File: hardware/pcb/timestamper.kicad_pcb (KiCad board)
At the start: 2 copper layers, 75 x 100 mm, 111 parts, among them J1 Conn_Coaxial, J2 Conn_Coaxial, J3 Conn_Coaxial, J4 JTAG, J5 ISP, J6 Conn_Coaxial, J7 USB_B_Micro, U1 AP1117-33, U10 ATMEGA328-AU, U11 74HC04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

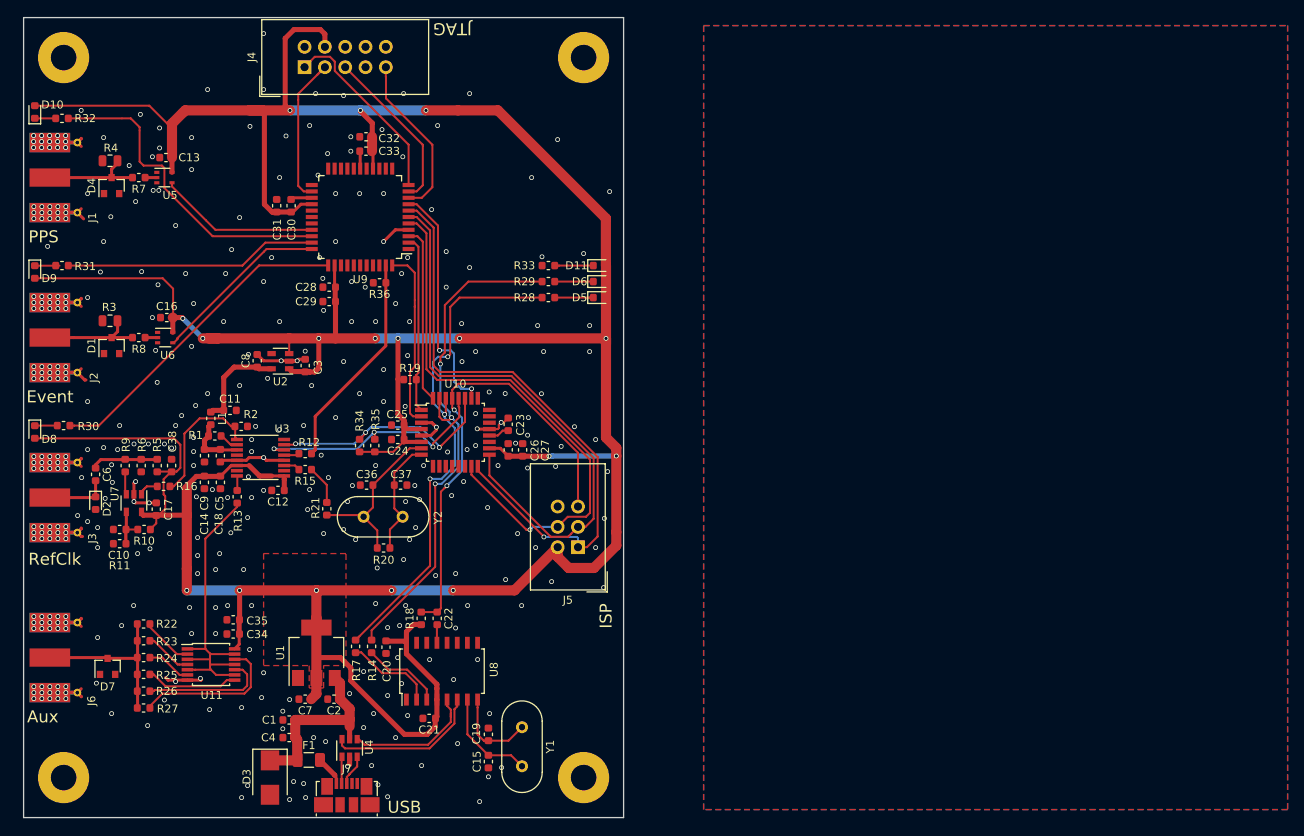
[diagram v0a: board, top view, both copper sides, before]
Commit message: Added silk-screen comments
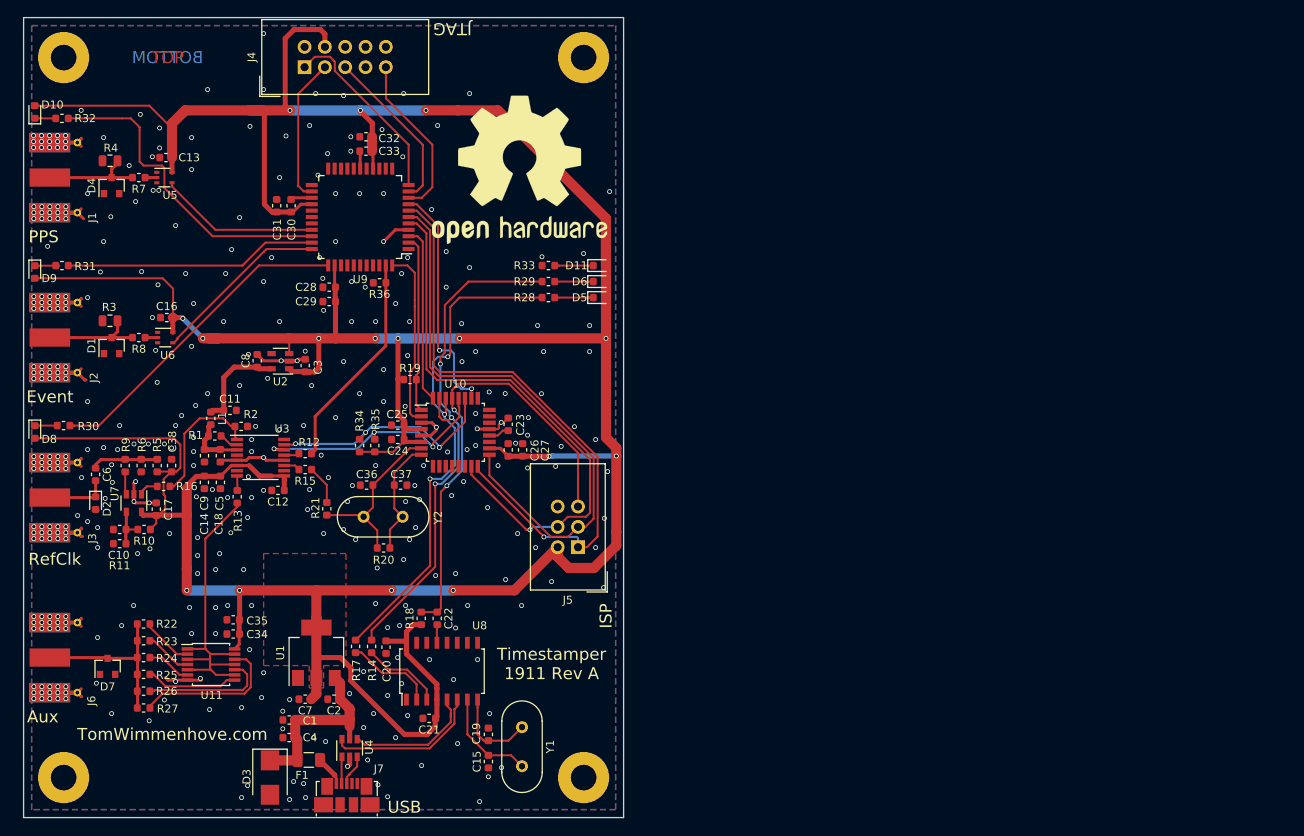
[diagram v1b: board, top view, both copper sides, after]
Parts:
- added REF**: OSHW-Logo2_24.3x20mm_SilkScreen, Symbol:OSHW-Logo2_24.3x20mm_SilkScreen, F.Cu at (112.0, 69.0)
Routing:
- net +3V3: vias 17 -> 16
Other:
- board text added: "BOTTOM"
- board text added: "TOP"
- board text added: "Timestamper 1911 Rev A"
- board text added: "TomWimmenhove.com"

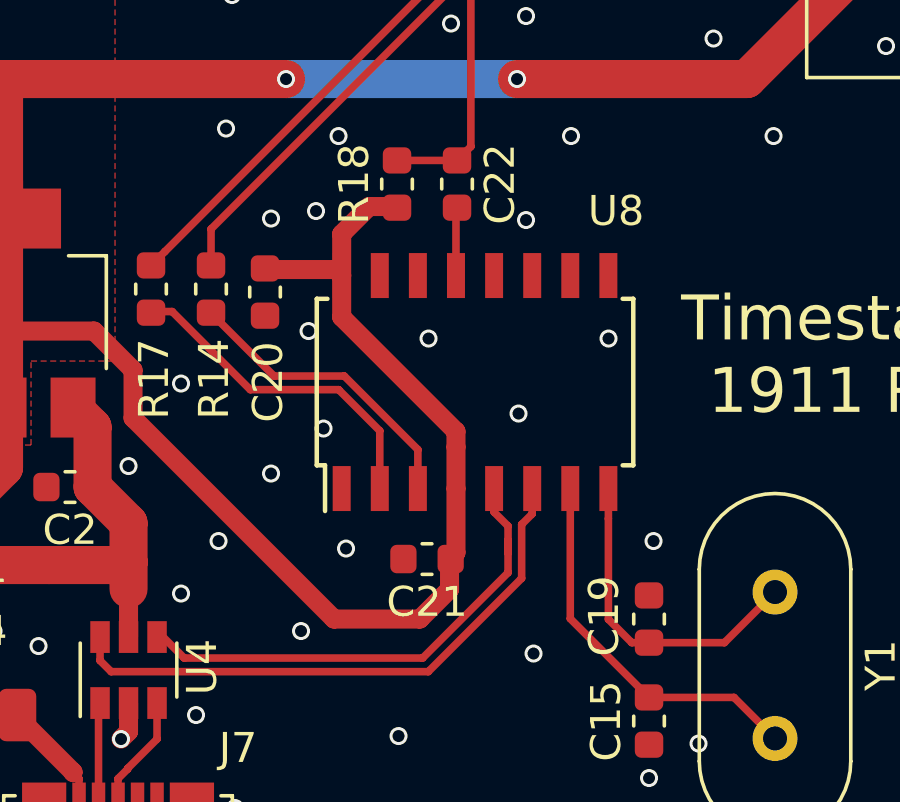
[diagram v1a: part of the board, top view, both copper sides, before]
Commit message: Fixed CH340G (U8) foot print
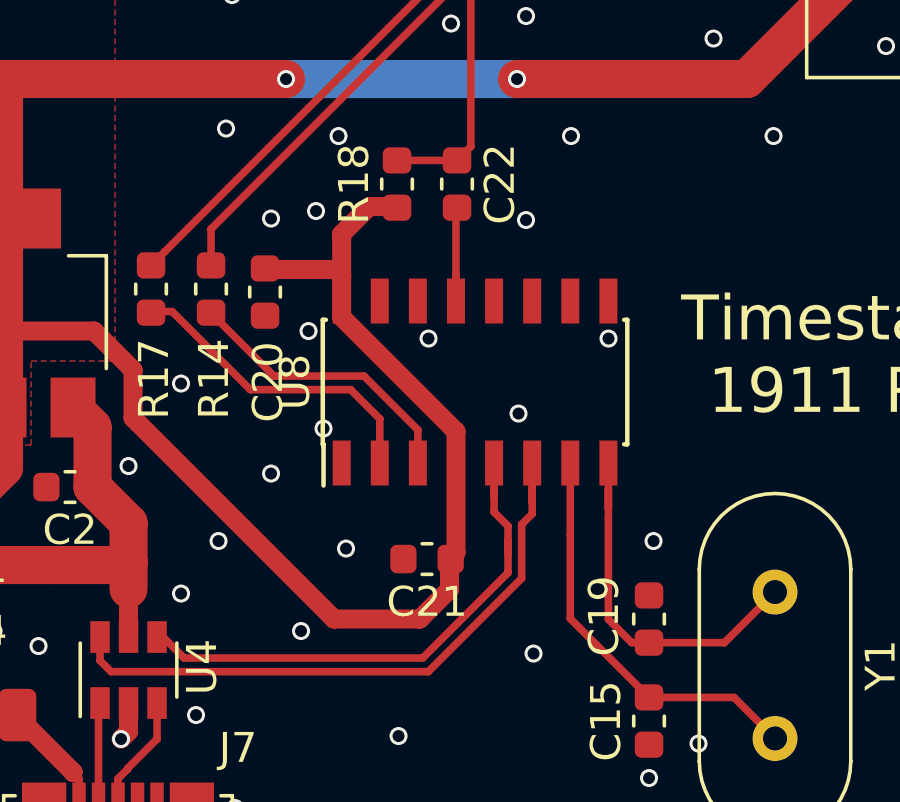
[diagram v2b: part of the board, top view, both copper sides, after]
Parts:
- U8: footprint Package_SO:SOIC-16W_5.3x10.2mm_P1.27mm -> Package_SO:SOIC-16_3.9x9.9mm_P1.27mm
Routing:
- net Net-(C19-Pad2): track 10.9 -> 12.4 mm
- net /USB_DM: track 19.4 -> 20.7 mm
- net /USB_DP: track 16.9 -> 18.0 mm
- net Net-(C22-Pad2): track 2.28 -> 3.13 mm
- net Net-(C15-Pad2): track 12.8 -> 13.7 mm
- net Net-(R17-Pad1): track 11.2 -> 10.6 mm

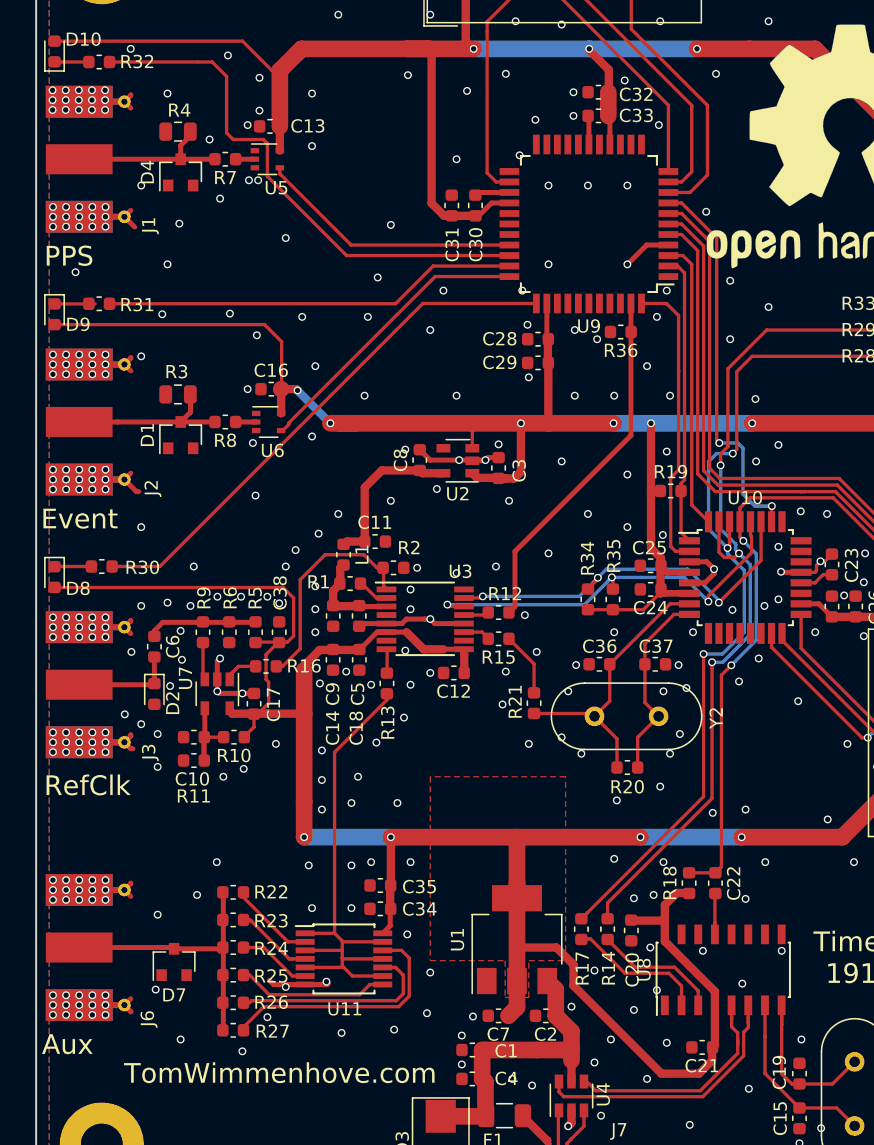
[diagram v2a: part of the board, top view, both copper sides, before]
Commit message: Added optional schmitt input on refclk
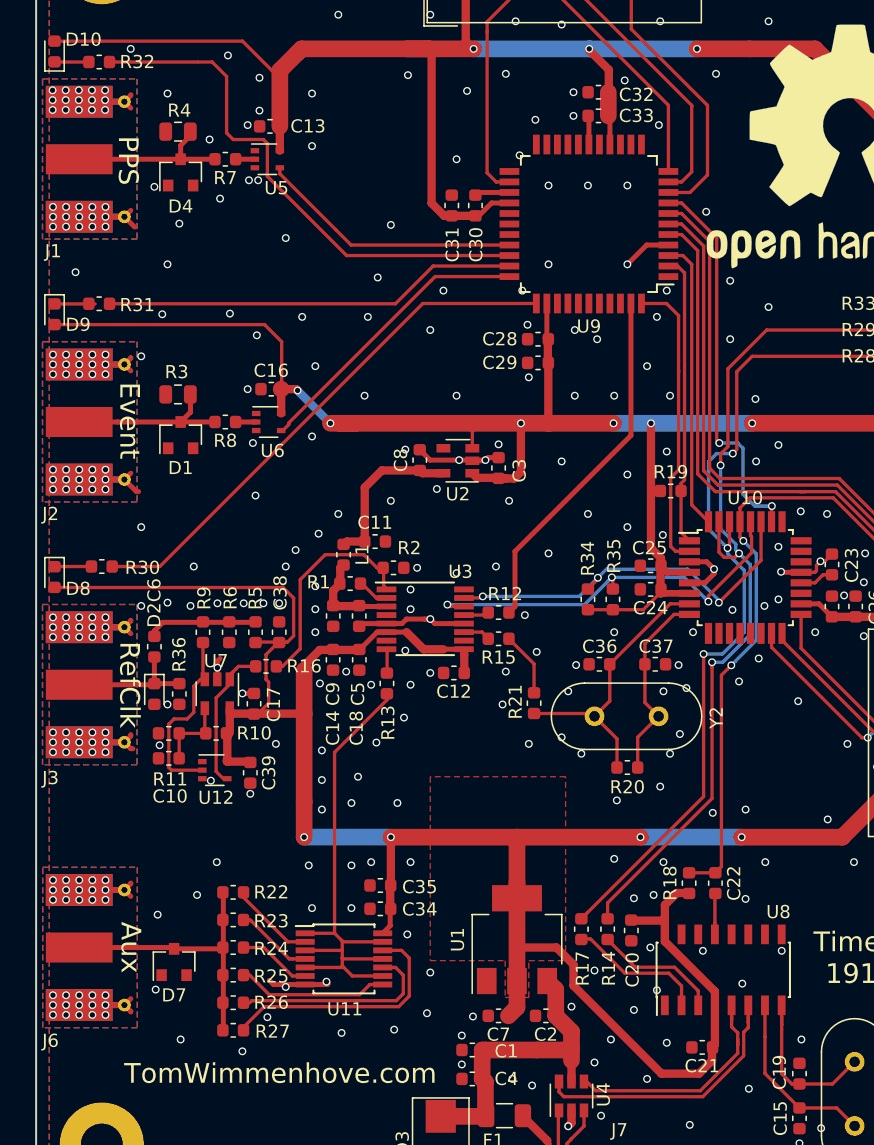
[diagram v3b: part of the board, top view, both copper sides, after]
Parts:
- added C39: C, Capacitor_SMD:C_0603_1608Metric, F.Cu at (66.3, 116.7)
- added U12: 74AHC1G14, Package_TO_SOT_SMD:SOT-353_SC-70-5, F.Cu at (63.6, 116.5)
- moved R36 43.5 mm to (60.9, 110.7), turned to 270 degrees
- moved R11 2.81 mm to (60.1, 113.7)
- moved C10 2.50 mm to (60.1, 115.6)
- moved R10 1.39 mm to (63.7, 113.7)
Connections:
- R36 pad 1: /MCLK_100MHZ -> Net-(C6-Pad2)
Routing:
- net Net-(R9-Pad1): track 2.68 -> 14.0 mm
- net Net-(R16-Pad2): track 2.77 -> 11.3 mm
- net +3V3: track 512.5 -> 516.3 mm
- net Net-(C10-Pad1): track 9.15 -> 5.99 mm
- net GND: track 58.1 -> 55.2 mm, vias 378 -> 371
- net Net-(C6-Pad2): track 7.78 -> 9.68 mm

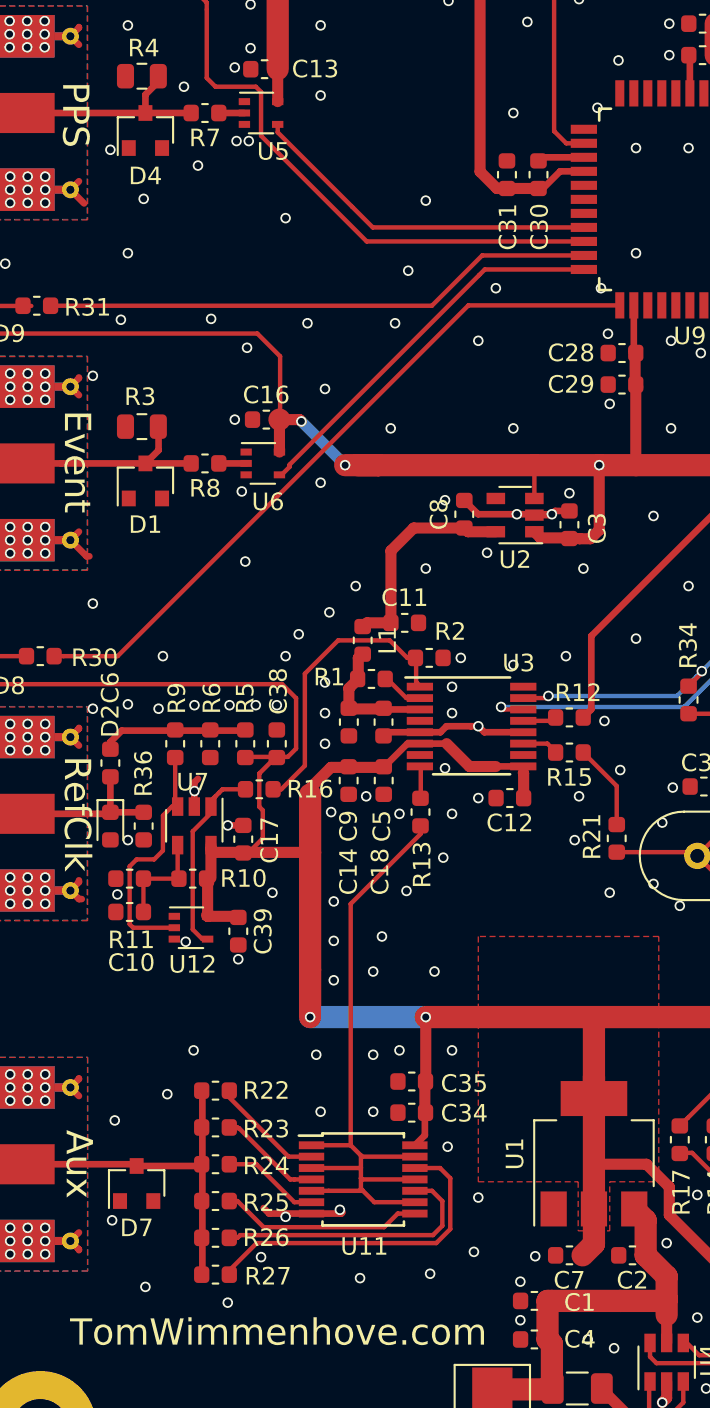
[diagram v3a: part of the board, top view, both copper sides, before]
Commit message: Added optional schmitt input on refclk
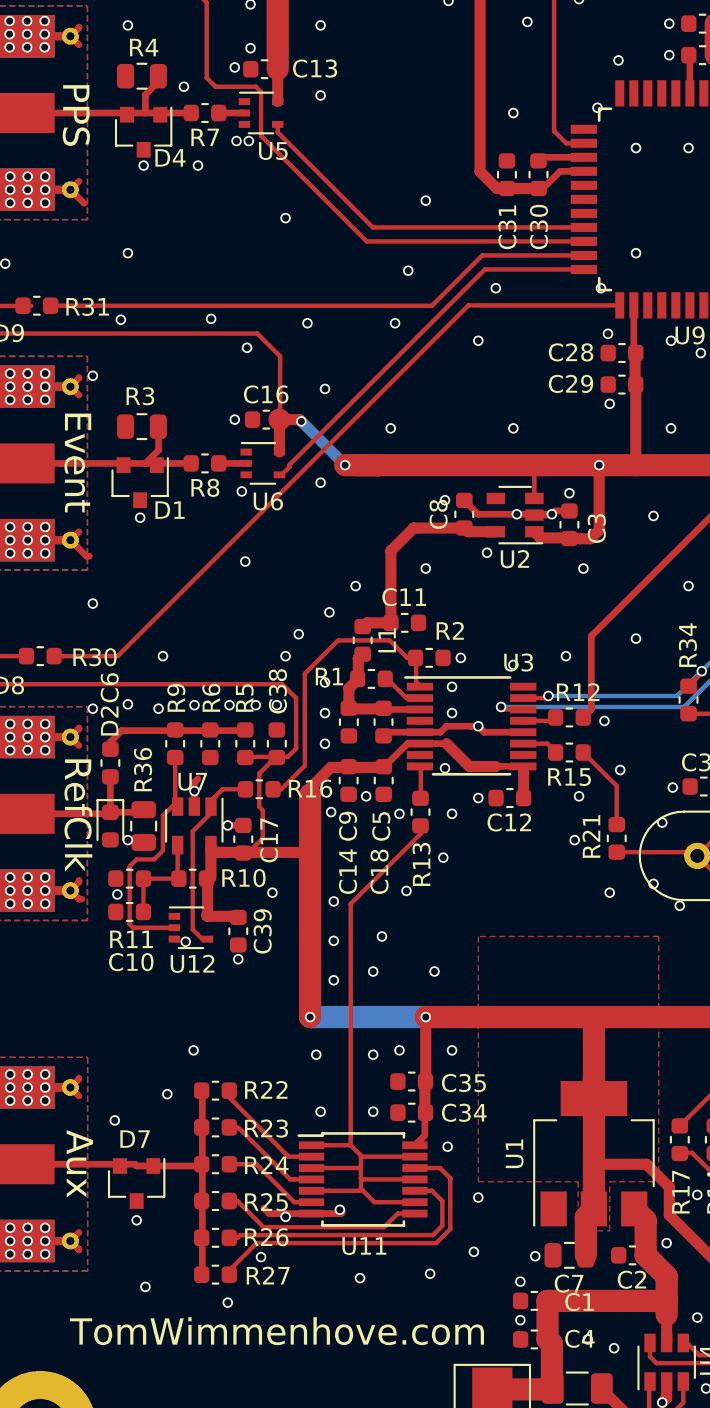
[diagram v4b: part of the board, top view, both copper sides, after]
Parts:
- C1, C10, C11, C12, C13, C14, C16, C17, C18, C22, C24, C26, C27, C29, C30, C31, C33, C34, C38, C39, C4, C5: value C -> 100n
- C15, C19, C36, C37: value C -> 22p
- C25, C28, C32, C9: value C -> 10n
- C35: value C -> 1u
- C7: footprint Capacitor_SMD:C_0603_1608Metric -> Capacitor_SMD:C_0805_2012Metric
- D1, D4: value D_Zener -> PESD5V2S2UT; footprint Diode_SMD:D_SOT-23_ANK -> Diode_SMD:D_SOT-23_NKA
- D2: value D_TVS -> PESD5V0U2BTTVS
- D3: value D_Zener -> 5v6
- D7: value D_Zener -> PESD3V3S2UT; footprint Diode_SMD:D_SOT-23_ANK -> Diode_SMD:D_SOT-23_NKA
- R1, R10, R11, R18, R19: value R -> 10k
- R12, R13, R15: value R -> 33
- R14, R17, R5, R6, R7, R8, R9: value R -> 100
- R20: value R -> 100k
- R22, R23, R24, R25, R26, R27: value R -> 270
- R28, R29, R30, R31, R32, R33: value R -> 330
- R3, R4: value R -> 51
- R34, R35: value R -> 2k2
- R36: value R -> 51; footprint Resistor_SMD:R_0603_1608Metric -> Resistor_SMD:R_0805_2012Metric
- moved D1 0.32 mm to (60.7, 91.1), turned to 270 degrees
- moved D4 0.14 mm to (60.9, 71.1), turned to 270 degrees
- turned D7 to 270 degrees
